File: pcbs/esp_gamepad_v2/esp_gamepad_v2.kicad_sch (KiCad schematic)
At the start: 70 parts, among them P1 USB_C_Plug_USB2.0, Q1 SI2300, SW1 SW_Push, SW10 SW_Push, SW11 DIP, SW12 SW_Push, SW13 SW_Push, SW14 SW_Push, SW2 SW_Push, SW3 SW_Push, SW4 SW_Push, SW5 SW_Push, SW6 SW_Push, SW7 SW_Push, SW8 SW_Push, SW9 SW_Push, U3 COM-09032, U5 LC709203FQH-02TWG, U6 COM-09032, U7 IP5306

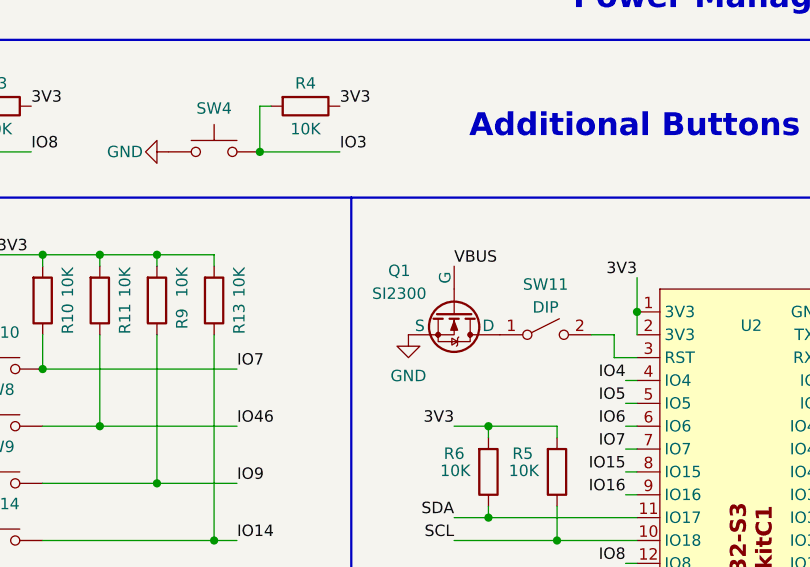
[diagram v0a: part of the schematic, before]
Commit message: pcb foorprint bug fixing
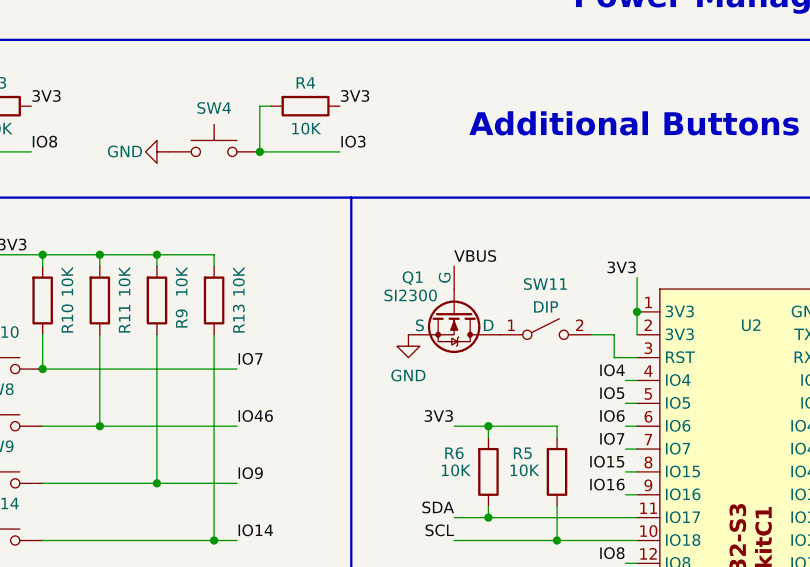
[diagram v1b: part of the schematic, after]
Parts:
- P1: footprint USB_Type_C:USB_Type_C_6P -> Connector_USB:USB_C_Receptacle_GCT_USB4125-xx-x-0190_6P_TopMnt_Horizontal
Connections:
- net GND: now also Q1.2 (S); no longer Q1.3 (S)
- net VBUS: now also Q1.1 (G); no longer Q1.2 (G)
- net at SW11.1 (A): now also Q1.3 (D); no longer Q1.1 (D)
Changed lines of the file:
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@@
 			)
 		)
-		(property "Footprint" "USB_Type_C:USB_Type_C_6P"
+		(property "Footprint" "Connector_USB:USB_C_Receptacle_GCT_USB4125-xx-x-0190_6P_TopMnt_Horizontal"
 			(at 39.37 36.83 0)
 			(effects
@@
 		(dnp no)
 		(property "Reference" "Q1"
-			(at 124.714 91.948 90)
+			(at 126.238 92.71 90)
 			(effects
 				(font
@@
 		)
 		(property "Value" "SI2300"
-			(at 124.714 94.488 90)
+			(at 125.984 94.742 90)
 			(effects
 				(font
@@
 		)
 		(property "Footprint" "Package_TO_SOT_SMD:SOT-23_Handsoldering"
-			(at 133.35 101.6 0)
+			(at 108.712 98.552 0)
 			(effects
 				(font
@@
 		)
 		(property "Description" "N-MOSFET transistor, drain/source/gate"
-			(at 130.81 96.52 0)
-			(effects
-				(font
+			(at 106.172 93.472 0)
+			(effects
+				(font
